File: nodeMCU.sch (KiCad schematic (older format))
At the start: 33 parts

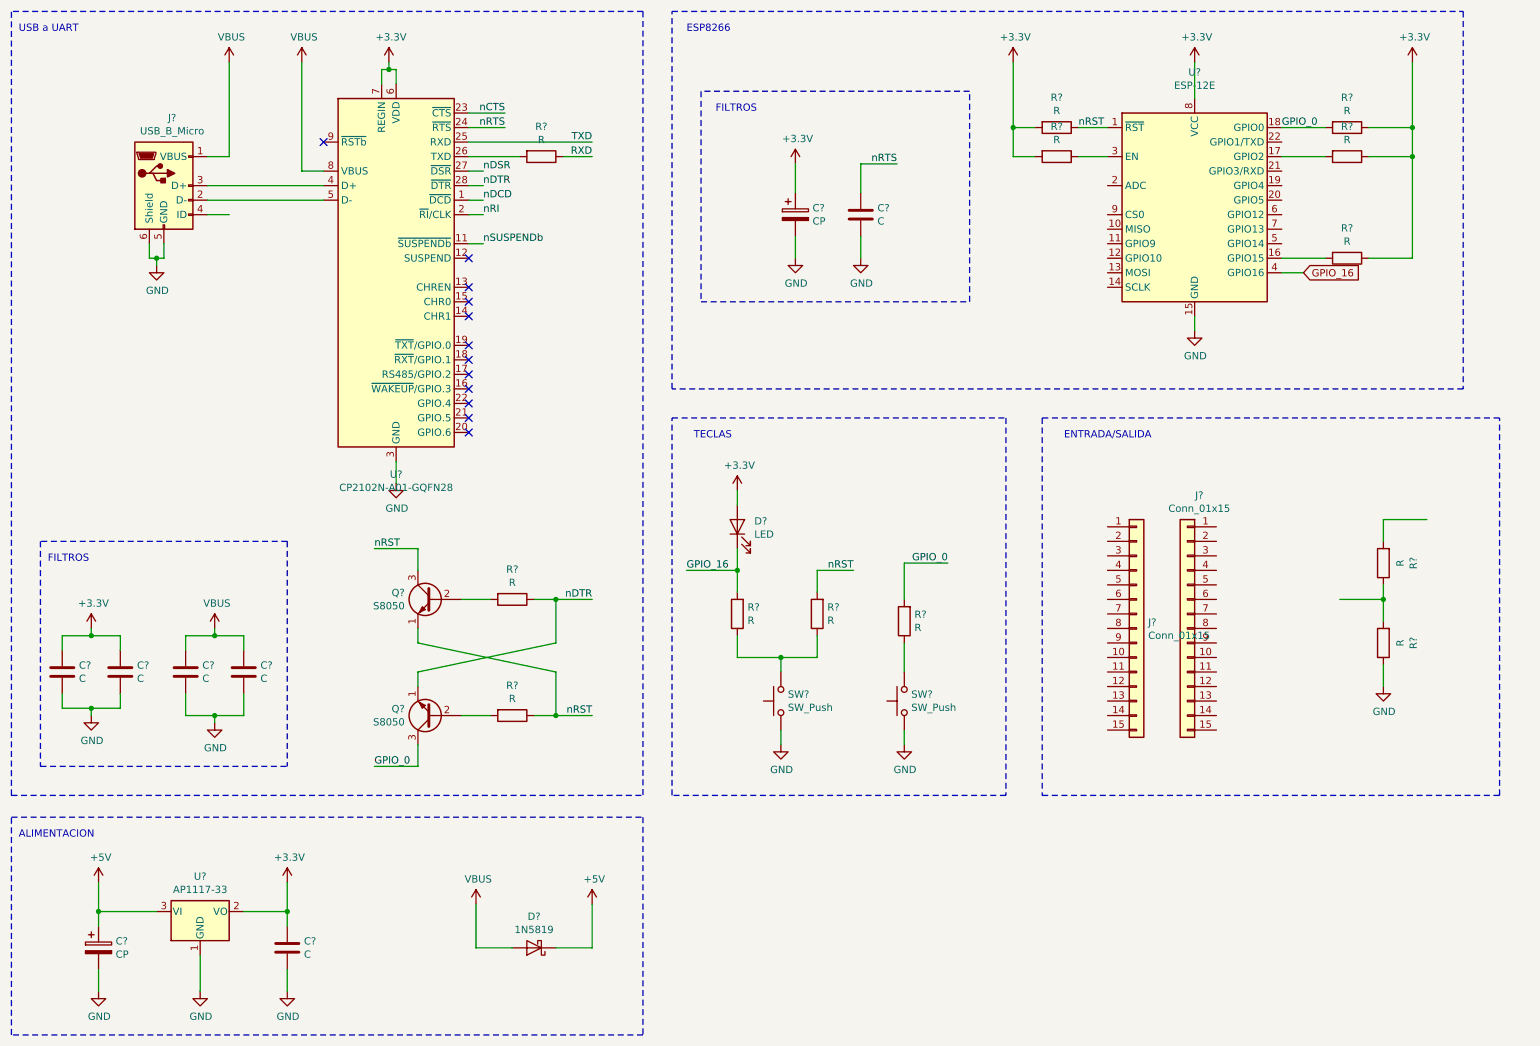
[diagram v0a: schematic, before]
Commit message: Primera version de esquematico terminada
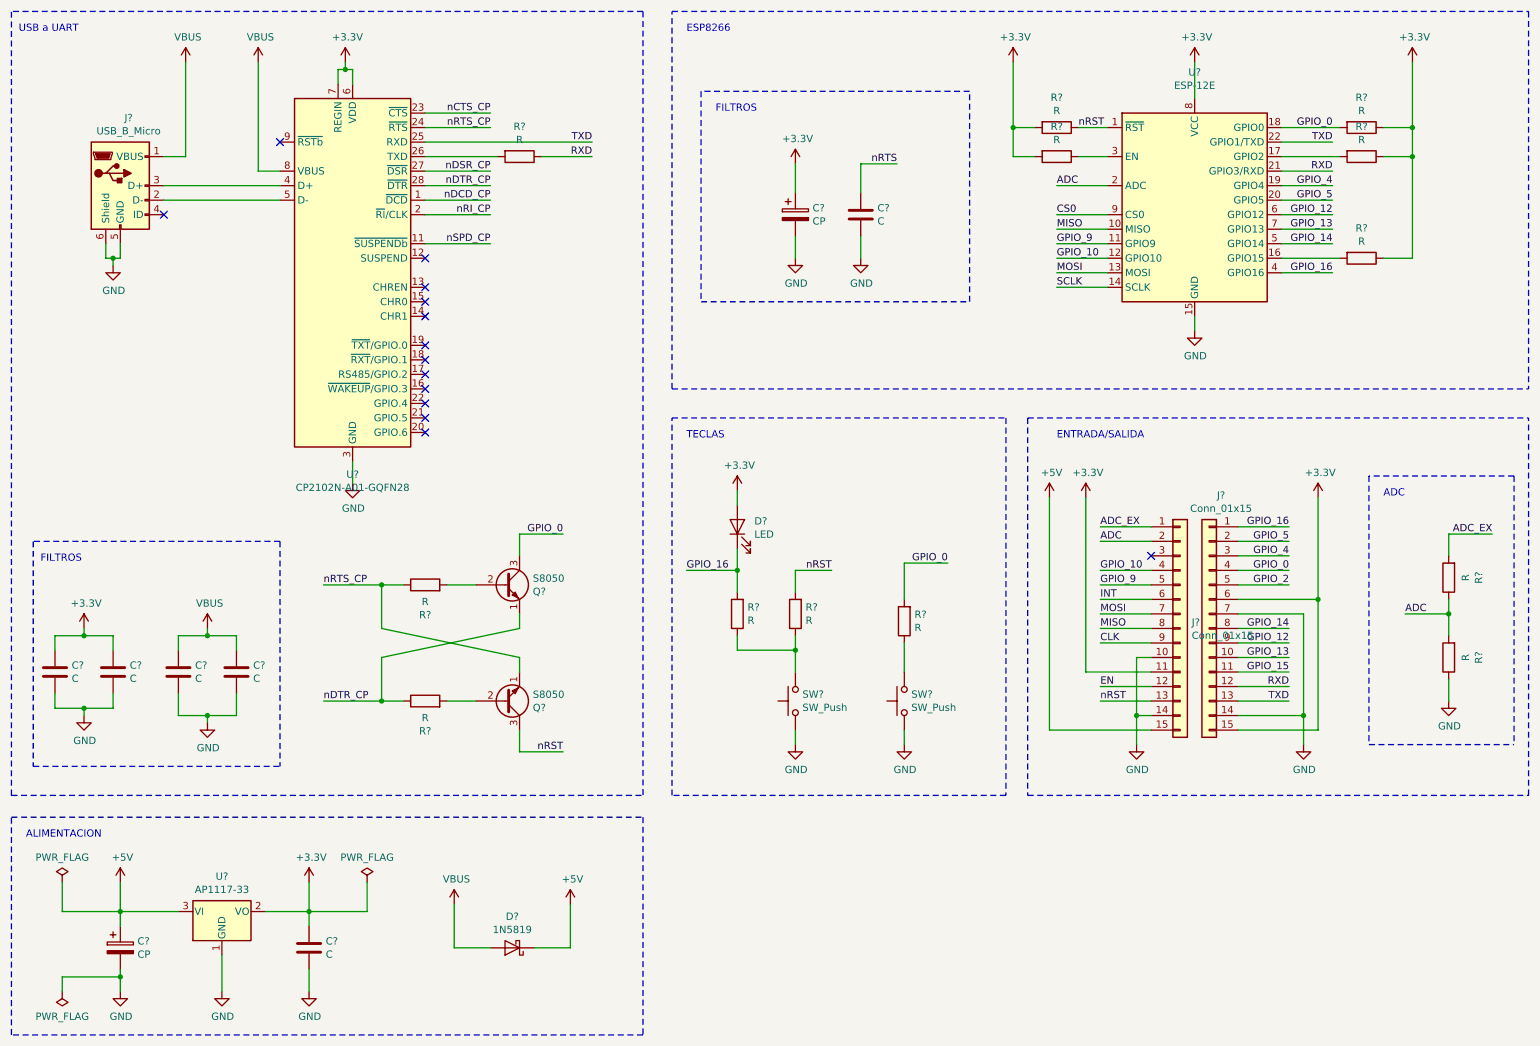
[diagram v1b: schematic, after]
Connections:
- net +3V3: now also J?.11 (Pin_11), J?.15 (Pin_15), J?.6 (Pin_6)
- net +5V: now also J?.15 (Pin_15)
- net GND: now also J?.10 (Pin_10), J?.14 (Pin_14), J?.14 (Pin_14), J?.7 (Pin_7)
- net GPIO_0: now also J?.4 (Pin_4)
- net GPIO_16: now also J?.1 (Pin_1)
- net RXD: now also J?.12 (Pin_12), U?.21 (GPIO3/RXD)
- net TXD: now also J?.13 (Pin_13), U?.22 (GPIO1/TXD)
- net nRST: now also J?.13 (Pin_13); no longer Q?.1 (E), R?.1
- net nRTS: no longer U?.24 (~RTS)
- net MISO: now reaches U?.10 (MISO)
- net MISO: now also J?.8 (Pin_8)
- net GPIO_9: now reaches U?.11 (GPIO9)
- net GPIO_9: now also J?.5 (Pin_5)
- net GPIO_10: now reaches U?.12 (GPIO10)
- net GPIO_10: now also J?.4 (Pin_4)
- net MOSI: now reaches U?.13 (MOSI)
- net MOSI: now also J?.7 (Pin_7)
- net SCLK: now reaches U?.14 (SCLK)
- net GPIO_4: now reaches U?.19 (GPIO4)
- net GPIO_4: now also J?.3 (Pin_3)
- net ADC: now reaches U?.2 (ADC)
- net ADC: now also J?.2 (Pin_2), R?.1, R?.2
- net GPIO_5: now reaches U?.20 (GPIO5)
- net GPIO_5: now also J?.2 (Pin_2)
- net GPIO_14: now reaches U?.5 (GPIO14)
- net GPIO_14: now also J?.8 (Pin_8)
- net GPIO_12: now reaches U?.6 (GPIO12)
- net GPIO_12: now also J?.9 (Pin_9)
- net GPIO_13: now reaches U?.7 (GPIO13)
- net GPIO_13: now also J?.10 (Pin_10)
- net CS0: now reaches U?.9 (CS0)
- net GPIO_15: now reaches J?.11 (Pin_11)
- net GPIO_2: now reaches J?.5 (Pin_5)
- net ADC_EX: now reaches J?.1 (Pin_1)
- net ADC_EX: now also R?.2
- net EN: now reaches J?.12 (Pin_12)
- net INT: now reaches J?.6 (Pin_6)
- net CLK: now reaches J?.9 (Pin_9)
- net nCTS renamed nCTS_CP
- net nDCD renamed nDCD_CP
- net nDSR renamed nDSR_CP
- net nDTR renamed nDTR_CP
- net nRI renamed nRI_CP
- net nSUSPENDb renamed nSPD_CP
- new net nRTS_CP: Q?.1 (E), R?.1, U?.24 (~RTS)
- no-connect marks 12 -> 14
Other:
- note added: "ADC"
- moved on the sheet: C?, D?, J?, Q?, R?, SW?, U?

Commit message: Terminada la revision 1.1 + rule check
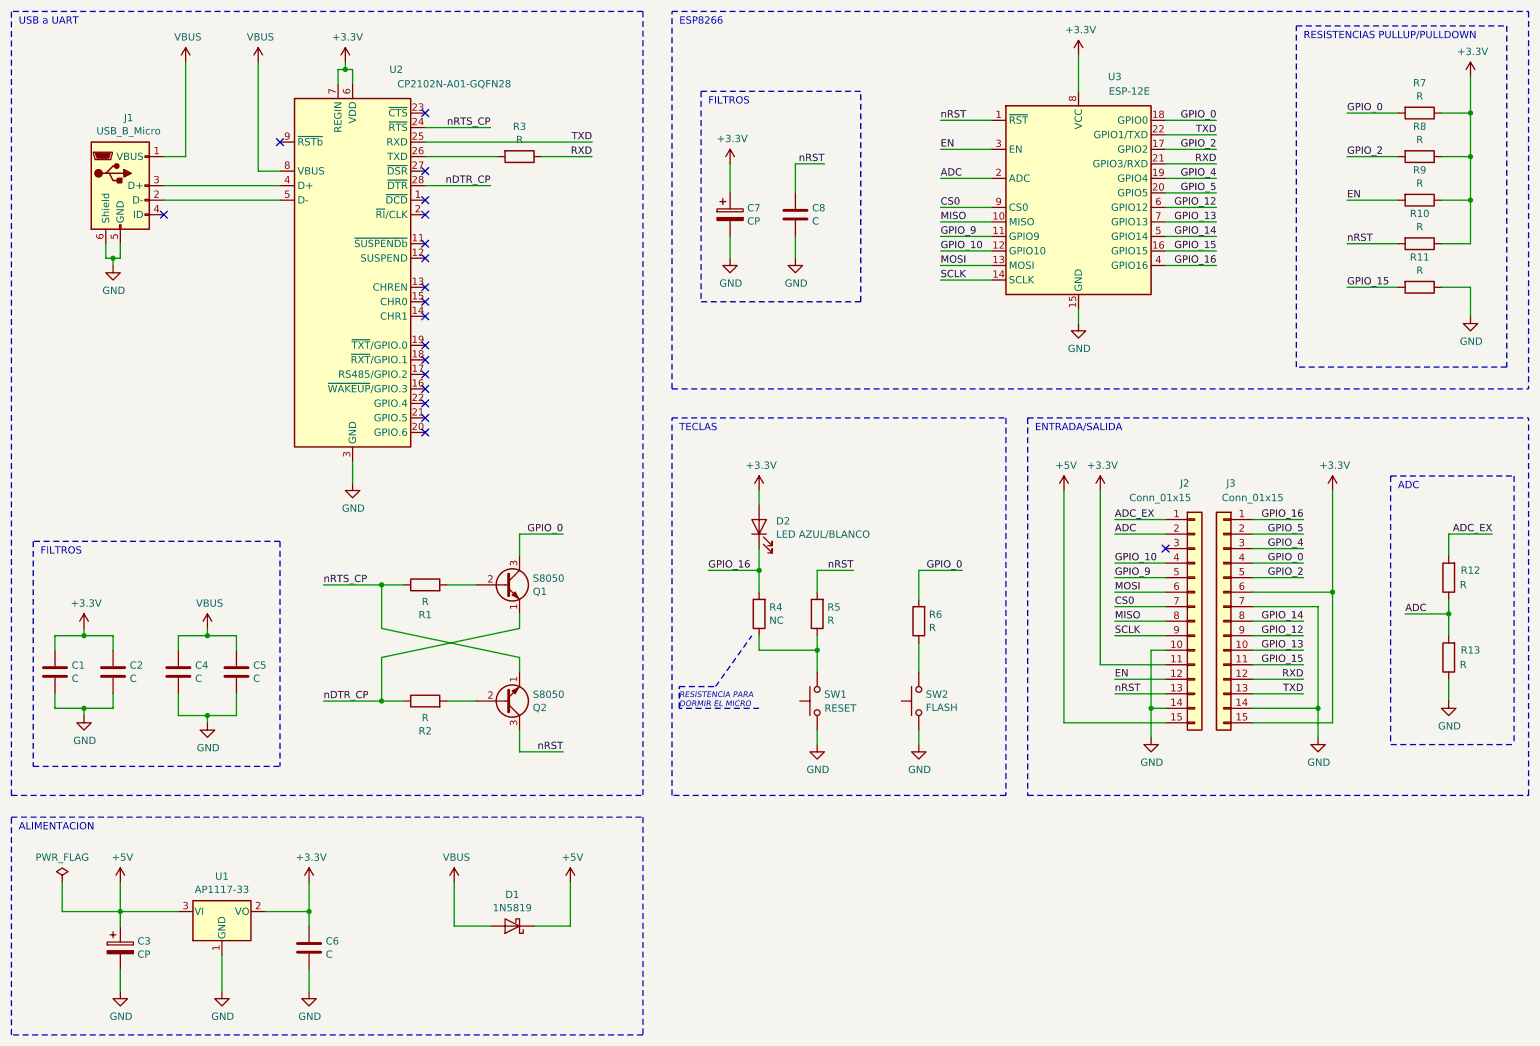
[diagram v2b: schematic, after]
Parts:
- removed R? (x5): R, symbol Device:R
- added R10, R11, R7, R8, R9: R, symbol Device:R
- D2: renamed from D?; value LED -> LED AZUL/BLANCO
- R4: renamed from R?; value R -> NC
- SW1: renamed from SW?; value SW_Push -> RESET
- SW2: renamed from SW?; value SW_Push -> FLASH
- gave numbers to parts that had none: 24
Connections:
- net CLK is gone; now on net SCLK: J2.9 (Pin_9)
- net INT is gone; now on net MOSI: J2.6 (Pin_6)
- net nRTS is gone; now on net nRST: C8.1
- net +3V3: now also R10.1, R7.1, R8.1, R9.1
- net CS0: now also J2.7 (Pin_7)
- net EN: now also U3.3 (EN), R9.2
- net GND: now also R11.1
- net GPIO_0: now also R7.2
- net GPIO_15: now also U3.16 (GPIO15), R11.2
- net GPIO_2: now also U3.17 (GPIO2), R8.2
- net MOSI: no longer J2.7 (Pin_7)
- net nRST: now also R10.2
- net nCTS_CP: no longer names the net of U2.23 (~CTS)
- net nDCD_CP: no longer names the net of U2.1 (~DCD)
- net nDSR_CP: no longer names the net of U2.27 (~DSR)
- net nRI_CP: no longer names the net of U2.2 (~RI~/CLK)
- net nSPD_CP: no longer names the net of U2.11 (~SUSPENDb)
- no-connect marks 14 -> 19
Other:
- note added: "RESISTENCIA PARA \nDORMIR EL MICRO"
- note added: "RESISTENCIAS PULLUP/PULLDOWN"
- moved on the sheet: C7, C8, D1, D2, J2, J3, R4, R5, R6, SW1, SW2, U3

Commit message: Agrego valores a los componentes
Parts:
- added R5: 0(NC), symbol Device:R
- C1, C4, C6: value C -> 10uF
- C2, C5, C8: value C -> 100nF
- C3: value CP -> 10uF/25v
- C7: value CP -> 100uF
- D2: value LED AZUL/BLANCO -> AZUL/BLANCO
- R1, R2: value R -> 12k
- R10: renamed from R9; value R -> 12k
- R11: renamed from R10; value R -> 12k
- R12: renamed from R11; value R -> 12k
- R13: renamed from R12; value R -> 220k(1%)
- R14: renamed from R13; value R -> 100k(1%)
- R3: value R -> 470
- R4: value NC -> 470
- R6: renamed from R5; value R -> 470
- R7: renamed from R6; value R -> 470
- R8: renamed from R7; value R -> 12k
- R9: renamed from R8; value R -> 12k
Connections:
- net +3V3: now also R4.2; no longer D2.2 (A)
- net GPIO_16: now also R5.2; no longer R4.2
- net at R6.1, SW1.2: now also R5.1; no longer R4.1
- new net: D2.2 (A), R4.1
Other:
- moved on the sheet: D2, R13, R14, R6, R7, SW1, SW2

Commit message: Agrego footprints
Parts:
- C1, C2, C4, C5, C6, C8: footprint (none) -> Capacitor_SMD:C_0402_1005Metric
- C3: footprint (none) -> Capacitor_SMD:C_0805_2012Metric
- C7: footprint (none) -> Capacitor_Tantalum_SMD:CP_EIA-3528-21_Kemet-B
- D2: footprint (none) -> LED_SMD:LED_0603_1608Metric
- J1: footprint (none) -> Connector_USB:USB_Micro-B_Amphenol_10103594-0001LF_Horizontal
- J2, J3: footprint (none) -> Connector_PinHeader_2.54mm:PinHeader_1x15_P2.54mm_Vertical
- Q1, Q2: footprint Package_TO_SOT_THT:TO-92_Inline -> Package_TO_SOT_SMD:SOT-23
- R1, R10, R11, R12, R13, R14, R2, R3, R4, R5, R6, R7, R8, R9: footprint (none) -> Resistor_SMD:R_0402_1005Metric
- SW1, SW2: footprint (none) -> Button_Switch_SMD:SW_Push_SPST_NO_Alps_SKRK
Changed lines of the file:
@@
 F 0 "C8" H 6115 2096 50  0000 L CNN
 F 1 "100nF" H 6115 2005 50  0000 L CNN
-F 2 "" H 6038 1900 50  0001 C CNN
+F 2 "Capacitor_SMD:C_0402_1005Metric" H 6038 1900 50  0001 C CNN
 F 3 "~" H 6000 2050 50  0001 C CNN
 	1    6000 2050
@@
 F 0 "Q2" H 4191 5446 50  0000 L CNN
 F 1 "S8050" H 4191 5355 50  0000 L CNN
-F 2 "Package_TO_SOT_THT:TO-92_Inline" H 4200 5325 50  0001 L CIN
+F 2 "Package_TO_SOT_SMD:SOT-23" H 4200 5325 50  0001 L CIN
 F 3 "http://www.unisonic.com.tw/datasheet/S8050.pdf" H 4000 5400 50  0001 L CNN
 	1    4000 5400
@@
 F 0 "Q1" H 4191 4554 50  0000 L CNN
 F 1 "S8050" H 4191 4645 50  0000 L CNN
-F 2 "Package_TO_SOT_THT:TO-92_Inline" H 4200 4525 50  0001 L CIN
+F 2 "Package_TO_SOT_SMD:SOT-23" H 4200 4525 50  0001 L CIN
 F 3 "http://www.unisonic.com.tw/datasheet/S8050.pdf" H 4000 4600 50  0001 L CNN
 	1    4000 4600
@@
 F 0 "R2" V 3243 5400 50  0000 C CNN
 F 1 "12k" V 3334 5400 50  0000 C CNN
-F 2 "" V 3380 5400 50  0001 C CNN
+F 2 "Resistor_SMD:R_0402_1005Metric" V 3380 5400 50  0001 C CNN
 F 3 "~" H 3450 5400 50  0001 C CNN
 	1    3450 5400
@@
 F 0 "R1" V 3243 4600 50  0000 C CNN
 F 1 "12k" V 3334 4600 50  0000 C CNN
-F 2 "" V 3380 4600 50  0001 C CNN
+F 2 "Resistor_SMD:R_0402_1005Metric" V 3380 4600 50  0001 C CNN
 F 3 "~" H 3450 4600 50  0001 C CNN
 	1    3450 4600
@@
 F 0 "C6" H 2765 7146 50  0000 L CNN
 F 1 "10uF" H 2765 7055 50  0000 L CNN
-F 2 "" H 2688 6950 50  0001 C CNN
+F 2 "Capacitor_SMD:C_0402_1005Metric" H 2688 6950 50  0001 C CNN
 F 3 "~" H 2650 7100 50  0001 C CNN
 	1    2650 7100
@@
 F 0 "C3" H 1468 7146 50  0000 L CNN
 F 1 "10uF/25v" H 1468 7055 50  0000 L CNN
-F 2 "" H 1388 6950 50  0001 C CNN
+F 2 "Capacitor_SMD:C_0805_2012Metric" H 1388 6950 50  0001 C CNN
 F 3 "~" H 1350 7100 50  0001 C CNN
 	1    1350 7100
@@
 F 0 "J3" H 8900 5800 50  0000 C CNN
 F 1 "Conn_01x15" H 8750 5700 50  0000 C CNN
-F 2 "" H 8950 4850 50  0001 C CNN
+F 2 "Connector_PinHeader_2.54mm:PinHeader_1x15_P2.54mm_Vertical" H 8950 4850 50  0001 C CNN
 F 3 "~" H 8950 4850 50  0001 C CNN
 	1    8950 4850
@@
 F 0 "J2" H 8650 5800 50  0000 L CNN
 F 1 "Conn_01x15" H 8300 5700 50  0000 L CNN
-F 2 "" H 8750 4850 50  0001 C CNN
+F 2 "Connector_PinHeader_2.54mm:PinHeader_1x15_P2.54mm_Vertical" H 8750 4850 50  0001 C CNN
 F 3 "~" H 8750 4850 50  0001 C CNN
 	1    8750 4850
@@
 F 0 "R3" V 4200 1650 50  0000 C CNN
 F 1 "470" V 4300 1650 50  0000 C CNN
-F 2 "" V 4030 1650 50  0001 C CNN
+F 2 "Resistor_SMD:R_0402_1005Metric" V 4030 1650 50  0001 C CNN
 F 3 "~" H 4100 1650 50  0001 C CNN
 	1    4100 1650
@@
 F 0 "C5" H 2265 5246 50  0000 L CNN
 F 1 "100nF" H 2265 5155 50  0000 L CNN
-F 2 "" H 2188 5050 50  0001 C CNN
+F 2 "Capacitor_SMD:C_0402_1005Metric" H 2188 5050 50  0001 C CNN
 F 3 "~" H 2150 5200 50  0001 C CNN
 	1    2150 5200
@@
 F 0 "C4" H 1865 5246 50  0000 L CNN
 F 1 "10uF" H 1865 5155 50  0000 L CNN
-F 2 "" H 1788 5050 50  0001 C CNN
+F 2 "Capacitor_SMD:C_0402_1005Metric" H 1788 5050 50  0001 C CNN
 F 3 "~" H 1750 5200 50  0001 C CNN
 	1    1750 5200
@@
 F 0 "C1" H 1015 5246 50  0000 L CNN
 F 1 "10uF" H 1015 5155 50  0000 L CNN
-F 2 "" H 938 5050 50  0001 C CNN
+F 2 "Capacitor_SMD:C_0402_1005Metric" H 938 5050 50  0001 C CNN
 F 3 "~" H 900 5200 50  0001 C CNN
 	1    900  5200
@@
 F 0 "C2" H 1415 5246 50  0000 L CNN
 F 1 "100nF" H 1415 5155 50  0000 L CNN
-F 2 "" H 1338 5050 50  0001 C CNN
+F 2 "Capacitor_SMD:C_0402_1005Metric" H 1338 5050 50  0001 C CNN
 F 3 "~" H 1300 5200 50  0001 C CNN
 	1    1300 5200
@@
 F 0 "R7" H 6880 4704 50  0000 R CNN
 F 1 "470" H 6880 4795 50  0000 R CNN
-F 2 "" V 6880 4750 50  0001 C CNN
+F 2 "Resistor_SMD:R_0402_1005Metric" V 6880 4750 50  0001 C CNN
 F 3 "~" H 6950 4750 50  0001 C CNN
 	1    6950 4750
@@
 F 0 "SW2" V 6996 5252 50  0000 R CNN
 F 1 "FLASH" V 6905 5252 50  0000 R CNN
-F 2 "" H 6950 5500 50  0001 C CNN
+F 2 "Button_Switch_SMD:SW_Push_SPST_NO_Alps_SKRK" H 6950 5500 50  0001 C CNN
 F 3 "~" H 6950 5500 50  0001 C CNN
 	1    6950 5300
@@
 F 0 "SW1" V 6346 5252 50  0000 R CNN
 F 1 "RESET" V 6250 5250 50  0000 R CNN
-F 2 "" H 6300 5500 50  0001 C CNN
+F 2 "Button_Switch_SMD:SW_Push_SPST_NO_Alps_SKRK" H 6300 5500 50  0001 C CNN
 F 3 "~" H 6300 5500 50  0001 C CNN
 	1    6300 5300
@@
 F 0 "D2" V 5850 4700 50  0000 R CNN
 F 1 "AZUL/BLANCO" V 5750 5100 50  0000 R CNN
-F 2 "" H 5800 4500 50  0001 C CNN
+F 2 "LED_SMD:LED_0603_1608Metric" H 5800 4500 50  0001 C CNN
 F 3 "~" H 5800 4500 50  0001 C CNN
 	1    5800 4500
@@
 F 0 "R13" H 10300 4500 50  0000 C CNN
 F 1 "220k(1%)" H 10200 4600 50  0000 C CNN
-F 2 "" V 10380 4550 50  0001 C CNN
+F 2 "Resistor_SMD:R_0402_1005Metric" V 10380 4550 50  0001 C CNN
 F 3 "~" H 10450 4550 50  0001 C CNN
 	1    10450 4550
@@
 F 0 "R14" H 10300 5050 50  0000 C CNN
 F 1 "100k(1%)" H 10200 5150 50  0000 C CNN
-F 2 "" V 10380 5100 50  0001 C CNN
+F 2 "Resistor_SMD:R_0402_1005Metric" V 10380 5100 50  0001 C CNN
 F 3 "~" H 10450 5100 50  0001 C CNN
 	1    10450 5100
@@
 F 0 "C7" H 5668 2096 50  0000 L CNN
 F 1 "100uF" H 5668 2005 50  0000 L CNN
-F 2 "" H 5588 1900 50  0001 C CNN
+F 2 "Capacitor_Tantalum_SMD:CP_EIA-3528-21_Kemet-B" H 5588 1900 50  0001 C CNN
 F 3 "~" H 5550 2050 50  0001 C CNN
 	1    5550 2050
@@
 F 0 "R8" V 10093 1350 50  0000 C CNN
 F 1 "12k" V 10184 1350 50  0000 C CNN
-F 2 "" V 10230 1350 50  0001 C CNN
+F 2 "Resistor_SMD:R_0402_1005Metric" V 10230 1350 50  0001 C CNN
 F 3 "~" H 10300 1350 50  0001 C CNN
 	1    10300 1350
@@
 F 0 "R9" V 10093 1650 50  0000 C CNN
 F 1 "12k" V 10184 1650 50  0000 C CNN
-F 2 "" V 10230 1650 50  0001 C CNN
+F 2 "Resistor_SMD:R_0402_1005Metric" V 10230 1650 50  0001 C CNN
 F 3 "~" H 10300 1650 50  0001 C CNN
 	1    10300 1650
@@
 F 0 "R10" V 10093 1950 50  0000 C CNN
 F 1 "12k" V 10184 1950 50  0000 C CNN
-F 2 "" V 10230 1950 50  0001 C CNN
+F 2 "Resistor_SMD:R_0402_1005Metric" V 10230 1950 50  0001 C CNN
 F 3 "~" H 10300 1950 50  0001 C CNN
 	1    10300 1950
@@
 F 0 "R11" V 10093 2250 50  0000 C CNN
 F 1 "12k" V 10184 2250 50  0000 C CNN
-F 2 "" V 10230 2250 50  0001 C CNN
+F 2 "Resistor_SMD:R_0402_1005Metric" V 10230 2250 50  0001 C CNN
 F 3 "~" H 10300 2250 50  0001 C CNN
 	1    10300 2250
@@
 F 0 "R12" V 10093 2550 50  0000 C CNN
 F 1 "12k" V 10184 2550 50  0000 C CNN
-F 2 "" V 10230 2550 50  0001 C CNN
+F 2 "Resistor_SMD:R_0402_1005Metric" V 10230 2550 50  0001 C CNN
 F 3 "~" H 10300 2550 50  0001 C CNN
 	1    10300 2550
@@
 F 0 "J1" H 1407 2317 50  0000 C CNN
 F 1 "USB_B_Micro" H 1407 2226 50  0000 C CNN
-F 2 "" H 1500 1800 50  0001 C CNN
+F 2 "Connector_USB:USB_Micro-B_Amphenol_10103594-0001LF_Horizontal" H 1500 1800 50  0001 C CNN
 F 3 "~" H 1500 1800 50  0001 C CNN
 	1    1350 1850
@@
 F 0 "R4" H 5730 3954 50  0000 R CNN
 F 1 "470" H 5730 4045 50  0000 R CNN
-F 2 "" V 5730 4000 50  0001 C CNN
+F 2 "Resistor_SMD:R_0402_1005Metric" V 5730 4000 50  0001 C CNN
 F 3 "~" H 5800 4000 50  0001 C CNN
 	1    5800 4000
@@
 F 0 "R5" V 5843 4950 50  0000 C CNN
 F 1 "0(NC)" V 5934 4950 50  0000 C CNN
-F 2 "" V 5980 4950 50  0001 C CNN
+F 2 "Resistor_SMD:R_0402_1005Metric" V 5980 4950 50  0001 C CNN
 F 3 "~" H 6050 4950 50  0001 C CNN
 	1    6050 4950
@@
 F 0 "R6" H 6230 4654 50  0000 R CNN
 F 1 "470" H 6230 4745 50  0000 R CNN
-F 2 "" V 6230 4700 50  0001 C CNN
+F 2 "Resistor_SMD:R_0402_1005Metric" V 6230 4700 50  0001 C CNN
 F 3 "~" H 6300 4700 50  0001 C CNN
 	1    6300 4700
